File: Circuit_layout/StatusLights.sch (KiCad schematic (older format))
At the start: 30 parts, among them Q1 ZVP4525G, U11 TLP293, U12 TLP293, U16 LTC3638, U2 PS2502-1, U25 TLP293

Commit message: modifying hvpl
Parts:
- removed R17: 250, symbol R
- removed R21: 150, symbol R
- removed U2: PS2502-1, symbol LTV-355T
- added C3: 2.2uF, Capacitors_SMD:C_0805_HandSoldering, symbol C
- added R76: 750k, Resistors_SMD:R_0805_HandSoldering, symbol R
- added R77: 196k, Resistors_SMD:R_0805_HandSoldering, symbol R
- added U1: PDM2-S24-S12, Converters_DCDC_ACDC:DCDC-Conv_TRACO_TMR_1-xxxx_Single, symbol PDM2-S24-S12
- L1: value 220uH -> 100uH; footprint (none) -> Inductors:Inductor_Taiyo-Yuden_NR-80xx_HandSoldering; Description (none) -> FIXED IND 100UH 1A 377 MOHM SMD; DigiKey P/N (none) -> 587-2004-1-ND; Man P/N (none) -> NR8040T101M; Price (none) -> 0.60; URL (none) -> https://www.digikey.com/product-detail/en/taiyo-yuden/NR804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
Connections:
- wire segments 94 -> 97
- no-connect marks 0 -> 1
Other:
- note added: "Need to verify DC DC Conv"
- note added: "Note: this is going to three LEDs"
- note added: "Outputs +12V"
- moved on the sheet: C19
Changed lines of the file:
@@
 LIBS:xilinx
 LIBS:Zilog
-LIBS:pacman-main-cache
 LIBS:bss84
 LIBS:+10v
@@
 Text Label 10250 2450 0    60   ~ 0
 Spare_Blue
-Text Label 8100 5800 2    60   ~ 0
-HVPL
 Text Notes 600  5000 0    60   ~ 0
 High Voltage
@@
 P 5600 5300
 F 0 "L1" V 5550 5300 50  0000 C CNN
-F 1 "220uH" V 5700 5300 50  0000 C CNN
-F 2 "" H 5600 5300 50  0001 C CNN
-F 3 "" H 5600 5300 50  0000 C CNN
+F 1 "100uH" V 5700 5300 50  0000 C CNN
+F 2 "Inductors:Inductor_Taiyo-Yuden_NR-80xx_HandSoldering" H 5600 5300 50  0001 C CNN
+F 3 "http://www.yuden.co.jp/productdata/catalog/en/wound04_e.pdf" H 5600 5300 50  0001 C CNN
+F 4 "587-2004-1-ND" V 5600 5300 60  0001 C CNN "DigiKey P/N"
+F 5 "https://www.digikey.com/product-detail/en/taiyo-yuden/NR8040T101M/587-2004-1-ND/1739117" V 5600 5300 60  0001 C CNN "URL"
+F 6 "NR8040T101M" V 5600 5300 60  0001 C CNN "Man P/N"
+F 7 "FIXED IND 100UH 1A 377 MOHM SMD" V 5600 5300 60  0001 C CNN "Description"
+F 8 "0.60" V 5600 5300 60  0001 C CNN "Price"
 	1    5600 5300
 	0    -1   -1   0
@@
 L C C19
 U 1 1 58BC115E
-P 6200 5750
-F 0 "C19" H 6225 5850 50  0000 L CNN
-F 1 "10uF" H 6225 5650 50  0000 L CNN
-F 2 "Capacitors_SMD:C_0805_HandSoldering" H 6238 5600 50  0001 C CNN
-F 3 "" H 6200 5750 50  0000 C CNN
-F 4 "490-10515-1-ND" H 6200 5750 60  0001 C CNN "DigiKey P/N"
-F 5 "http://www.digikey.com/product-detail/en/murata-electronics-north-america/GRM21BR6YA106ME43L/490-10515-1-ND/5026446" H 6200 5750 60  0001 C CNN "URL"
-F 6 "GRM21BR6YA106ME43L" H 6200 5750 60  0001 C CNN "Man P/N"
-	1    6200 5750
-	1    0    0    -1
-$EndComp
-$Comp
-L LTV-355T U2
-U 1 1 58C27110
-P 7150 5700
-F 0 "U2" H 6940 5890 50  0000 L CNN
-F 1 "PS2502-1" H 7150 5900 50  0000 L CNN
-F 2 "" H 6950 5500 50  0000 L CIN
-F 3 "http://www.cel.com/pdf/datasheets/ps2502.pdf" H 7150 5700 50  0001 L CNN
-F 4 "PS2502L-1-F3-ACT-ND" H 7150 5700 60  0001 C CNN "DigiKey P/N"
-F 5 "http://www.digikey.com/product-detail/en/cel/PS2502L-1-F3-A/PS2502L-1-F3-ACT-ND/3646234" H 7150 5700 60  0001 C CNN "URL"
-F 6 "PS2502L-1-F3-A" H 7150 5700 60  0001 C CNN "Man P/N"
-F 7 "OPTOISOLATOR 5KV DARL 4SMD" H 7150 5700 60  0001 C CNN "Description"
-F 8 "1.10" H 7150 5700 60  0001 C CNN "Price"
-	1    7150 5700
-	1    0    0    -1
-$EndComp
-$Comp
-L R R21
-U 1 1 58C2C36E
-P 7750 5600
-F 0 "R21" V 7830 5600 50  0000 C CNN
-F 1 "150" V 7750 5600 50  0000 C CNN
-F 2 "" V 7680 5600 50  0000 C CNN
-F 3 "" H 7750 5600 50  0000 C CNN
-	1    7750 5600
-	0    1    1    0
-$EndComp
-$Comp
-L +24V #PWR045
-U 1 1 58C2C48F
-P 8050 5500
-F 0 "#PWR045" H 8050 5350 50  0001 C CNN
-F 1 "+24V" H 8050 5640 50  0000 C CNN
-F 2 "" H 8050 5500 50  0000 C CNN
-F 3 "" H 8050 5500 50  0000 C CNN
-	1    8050 5500
-	1    0    0    -1
-$EndComp
-Text Notes 2950 8850 0    60   ~ 0
+P 6600 5750
+F 0 "C19" H 6625 5850 50  0000 L CNN
+F 1 "10uF" H 6625 5650 50  0000 L CNN
+F 2 "Capacitors_SMD:C_0805_HandSoldering" H 6638 5600 50  0001 C CNN
+F 3 "" H 6600 5750 50  0000 C CNN
+F 4 "490-10515-1-ND" H 6600 5750 60  0001 C CNN "DigiKey P/N"
+F 5 "http://www.digikey.com/product-detail/en/murata-electronics-north-america/GRM21BR6YA106ME43L/490-10515-1-ND/5026446" H 6600 5750 60  0001 C CNN "URL"
+F 6 "GRM21BR6YA106ME43L" H 6600 5750 60  0001 C CNN "Man P/N"
+	1    6600 5750
+	1    0    0    -1
+$EndComp
+Text Notes 3550 7400 0    60   ~ 0
 If want to go back to 24V\nsw - 750k - Vfb - 196k - gnd
-$Comp
-L R R17
-U 1 1 58C2FC44
-P 6550 5300
-F 0 "R17" V 6630 5300 50  0000 C CNN
-F 1 "250" V 6550 5300 50  0000 C CNN
-F 2 "" V 6480 5300 50  0000 C CNN
-F 3 "" H 6550 5300 50  0000 C CNN
-	1    6550 5300
-	0    1    1    0
-$EndComp
 Wire Wire Line
 	4250 1200 4350 1200
@@
 	5000 5700 4850 5700
 Wire Wire Line
-	4850 5300 5300 5300
-Wire Wire Line
-	5900 5300 6400 5300
-Wire Wire Line
-	6000 5500 4850 5500
-Wire Wire Line
 	4350 6200 4350 6100
-Wire Wire Line
-	6000 5300 6000 5500
 Wire Wire Line
 	5200 6200 5200 5900
 Connection ~ 5200 6200
-Wire Wire Line
-	5200 5300 5200 5600
-Connection ~ 5200 5300
-Connection ~ 6000 5300
 Wire Notes Line
 	450  4850 11250 4850
-Wire Wire Line
-	7450 5800 8100 5800
-Wire Wire Line
-	7450 5600 7600 5600
-Wire Wire Line
-	7900 5600 8050 5600
-Wire Wire Line
-	8050 5600 8050 5500
-Wire Wire Line
-	6200 6200 6200 5900
 Connection ~ 6200 6200
 Wire Wire Line
-	6200 5600 6200 5300
-Connection ~ 6200 5300
-Wire Wire Line
-	6700 5300 6800 5300
-Wire Wire Line
-	6800 5300 6800 5600
-Wire Wire Line
-	6800 5600 6850 5600
-Wire Wire Line
-	6850 5800 6800 5800
-Wire Wire Line
-	6800 5800 6800 6200
-Wire Wire Line
 	4800 3450 4800 3550
 Wire Wire Line
 	4800 3550 4950 3550
 $Comp
-L +24V #PWR046
+L +24V #PWR045
 U 1 1 58C523A5
 P 4800 2750
-F 0 "#PWR046" H 4800 2600 50  0001 C CNN
+F 0 "#PWR045" H 4800 2600 50  0001 C CNN
 F 1 "+24V" H 4800 2890 50  0000 C CNN
 F 2 "" H 4800 2750 50  0000 C CNN
@@
 $EndComp
 $Comp
-L GND #PWR047
+L GND #PWR046
 U 1 1 58C77294
 P 13700 3000
-F 0 "#PWR047" H 13700 2750 50  0001 C CNN
+F 0 "#PWR046" H 13700 2750 50  0001 C CNN
 F 1 "GND" H 13700 2850 50  0000 C CNN
 F 2 "" H 13700 3000 50  0000 C CNN
@@
 $EndComp
 $Comp
-L +24V #PWR048
+L +24V #PWR047
 U 1 1 58C7729A
 P 15100 2550
-F 0 "#PWR048" H 15100 2400 50  0001 C CNN
+F 0 "#PWR047" H 15100 2400 50  0001 C CNN
 F 1 "+24V" H 15100 2690 50  0000 C CNN
 F 2 "" H 15100 2550 50  0000 C CNN
@@
 HV-
 $Comp
-L PWR_FLAG #FLG049
+L PWR_FLAG #FLG048
 U 1 1 58C1AF3D
 P 3600 5200
-F 0 "#FLG049" H 3600 5295 50  0001 C CNN
+F 0 "#FLG048" H 3600 5295 50  0001 C CNN
 F 1 "PWR_FLAG" H 3600 5380 50  0000 C CNN
 F 2 "" H 3600 5200 50  0000 C CNN
@@
 Connection ~ 3600 5300
 Wire Wire Line
-	6800 6200 700  6200
+	700  6200 7150 6200
 $Comp
 L R R20
@@
 Wire Wire Line
 	1250 1400 1400 1400
+$Comp
+L R R77
+U 1 1 58D32889
+P 6200 5950
+F 0 "R77" V 6280 5950 50  0000 C CNN
+F 1 "196k" V 6200 5950 50  0000 C CNN
+F 2 "Resistors_SMD:R_0805_HandSoldering" V 6130 5950 50  0001 C CNN
+F 3 "" H 6200 5950 50  0000 C CNN
+F 4 "P196CCT-ND" V 6200 5950 60  0001 C CNN "DigiKey P/N"
+F 5 "http://www.digikey.com/product-detail/en/panasonic-electronic-components/ERJ-6ENF1960V/P196CCT-ND/118752" V 6200 5950 60  0001 C CNN "URL"
+F 6 "ERJ-6ENF1960V" V 6200 5950 60  0001 C CNN "Man P/N"
+F 7 "RES SMD 196 OHM 1% 1/8W 0805" V 6200 5950 60  0001 C CNN "Description"
+F 8 "0.1" V 6200 5950 60  0001 C CNN "Price"
+	1    6200 5950
+	1    0    0    -1
+$EndComp
+$Comp
+L R R76
+U 1 1 58D32960
+P 6200 5550
+F 0 "R76" V 6280 5550 50  0000 C CNN
+F 1 "750k" V 6200 5550 50  0000 C CNN
+F 2 "Resistors_SMD:R_0805_HandSoldering" V 6130 5550 50  0001 C CNN
+F 3 "" H 6200 5550 50  0000 C CNN
+F 4 "P750KCCT-ND" V 6200 5550 60  0001 C CNN "DigiKey P/N"
+F 5 "http://www.digikey.com/product-detail/en/panasonic-electronic-components/ERJ-6ENF7503V/P750KCCT-ND/119800" V 6200 5550 60  0001 C CNN "URL"
+F 6 "ERJ-6ENF7503V" V 6200 5550 60  0001 C CNN "Man P/N"
+F 7 "RES SMD 750K OHM 1% 1/8W 0805" V 6200 5550 60  0001 C CNN "Description"
+F 8 "0.1" V 6200 5550 60  0001 C CNN "Price"
+	1    6200 5550
+	1    0    0    -1
+$EndComp
+Wire Wire Line
+	6200 5700 6200 5800
+Wire Wire Line
+	4850 5300 5300 5300
+Wire Wire Line
+	5200 5600 5200 5300
+Connection ~ 5200 5300
+Wire Wire Line
+	5900 5300 7150 5300
+Wire Wire Line
+	6200 5300 6200 5400
+Wire Wire Line
+	6200 6100 6200 6200
+Connection ~ 6200 5300
+Wire Wire Line
+	6600 5300 6600 5600
+Wire Wire Line
+	6600 5900 6600 6200
+Connection ~ 6600 6200
+Connection ~ 6600 5300
+$Comp
+L PDM2-S24-S12 U1
+U 1 1 58D3B6C8
+P 7900 5700
+F 0 "U1" H 7900 5600 50  0000 C CNN
+F 1 "PDM2-S24-S12" H 7900 5900 50  0000 C CNN
+F 2 "Converters_DCDC_ACDC:DCDC-Conv_TRACO_TMR_1-xxxx_Single" H 7900 5300 50  0001 C CNN
+F 3 "" H 7900 5200 50  0001 C CNN
+F 4 "102-2728-ND" H 7900 5700 60  0001 C CNN "DigiKey P/N"
+F 5 "https://www.digikey.com/product-detail/en/cui-inc/PDM2-S24-S12-S/102-2728-ND/4009652" H 7900 5700 60  0001 C CNN "URL"
+F 6 "PDM2-S24-S12-S" H 7900 5700 60  0001 C CNN "Man P/N"
+F 7 "CONVERT DC/DC 2W 12V 167MA OUT" H 7900 5700 60  0001 C CNN "Description"
+	1    7900 5700
+	1    0    0    -1
+$EndComp
+Wire Wire Line
+	7150 5300 7150 5600
+Wire Wire Line
+	7150 5800 7150 5800
+Wire Wire Line
+	7150 6200 7150 5800
+NoConn ~ 8650 5700
+$Comp
+L GND #PWR049
+U 1 1 58D3C796
+P 9400 5950
+F 0 "#PWR049" H 9400 5700 50  0001 C CNN
+F 1 "GND" H 9400 5800 50  0000 C CNN
+F 2 "" H 9400 5950 50  0000 C CNN
+F 3 "" H 9400 5950 50  0000 C CNN
+	1    9400 5950
+	1    0    0    -1
+$EndComp
+Text Label 9500 5550 2    60   ~ 0
+HVPL
+Text Notes 8550 5400 0    60   ~ 0
+Note: this is going to three LEDs
+Text Notes 7350 6200 0    60   ~ 0
+Need to verify DC DC Conv
+$Comp
+L C C3
+U 1 1 58D40888
+P 9000 5700
+F 0 "C3" H 9025 5800 50  0000 L CNN
+F 1 "2.2uF" H 9025 5600 50  0000 L CNN
+F 2 "Capacitors_SMD:C_0805_HandSoldering" H 9038 5550 50  0001 C CNN
+F 3 "" H 9000 5700 50  0000 C CNN
+F 4 "587-1293-1-ND" H 9000 5700 60  0001 C CNN "DigiKey P/N"
+F 5 "http://www.digikey.com/product-detail/en/taiyo-yuden/EMK212BJ225KG-T/587-1293-1-ND/931070" H 9000 5700 60  0001 C CNN "URL"
+F 6 "EMK212BJ225KG-T" H 9000 5700 60  0001 C CNN "Man P/N"
+F 7 "CAP CER 2.2UF 16V X5R 0805" H 9000 5700 60  0001 C CNN "Description"
+	1    9000 5700
+	1    0    0    -1
+$EndComp
+Text Notes 7600 5350 0    60   ~ 0
+Outputs +12V
+Wire Wire Line
+	8650 5800 8650 5850
+Wire Wire Line
+	8650 5850 9400 5850
+Wire Wire Line
+	8650 5600 8650 5550
+Wire Wire Line
+	8650 5550 9500 5550
+Connection ~ 9000 5550
+Wire Wire Line
+	9400 5850 9400 5950
+Connection ~ 9000 5850
+Wire Wire Line
+	4850 5500 6000 5500
+Wire Wire Line
+	6000 5500 6000 5750
+Wire Wire Line
+	6000 5750 6200 5750
+Connection ~ 6200 5750
 $EndSCHEMATC

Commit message: added footprint to DPDT switch, test points, DRC passes
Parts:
- removed R75: 150, Resistors_SMD:R_0805_HandSoldering, symbol R
- removed U25: TLP293, Housings_SSOP:SOP-4_4.4x2.8mm_Pitch1.27mm, symbol TLP291
- added HVPL_HV: TEST_1P, Measurement_Points:Measurement_Point_Round-SMD-Pad_Big, symbol TEST_1P
- added W?: HVPL_LV, Measurement_Points:Measurement_Point_Round-SMD-Pad_Big, symbol TEST_1P
- added W?: GLV_GND, Measurement_Points:Measurement_Point_Square-SMD-Pad_Big, symbol TEST_1P
- added W?: HV_GND, Measurement_Points:Measurement_Point_Square-SMD-Pad_Big, symbol TEST_1P
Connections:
- net GND: now also W?.1
- net HV-: now also W?.1
- net HVPL: now also W?.1
- net at C19.1, L1.2, R76.1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: now also HVPL_HV.1
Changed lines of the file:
@@
 LIBS:xilinx
 LIBS:Zilog
+LIBS:pacman-main-cache
 LIBS:bss84
 LIBS:+10v
@@
 $EndComp
 $Comp
-L GND #PWR036
+L GND #PWR037
 U 1 1 58AF33D9
 P 4250 1300
-F 0 "#PWR036" H 4250 1050 50  0001 C CNN
+F 0 "#PWR037" H 4250 1050 50  0001 C CNN
 F 1 "GND" H 4250 1150 50  0000 C CNN
 F 2 "" H 4250 1300 50  0000 C CNN
@@
 $EndComp
 $Comp
-L +24V #PWR037
+L +24V #PWR038
 U 1 1 58AF3526
 P 5650 850
-F 0 "#PWR037" H 5650 700 50  0001 C CNN
+F 0 "#PWR038" H 5650 700 50  0001 C CNN
 F 1 "+24V" H 5650 990 50  0000 C CNN
 F 2 "" H 5650 850 50  0000 C CNN
@@
 $EndComp
 $Comp
-L GND #PWR038
+L GND #PWR039
 U 1 1 58AF4273
 P 4250 2500
-F 0 "#PWR038" H 4250 2250 50  0001 C CNN
+F 0 "#PWR039" H 4250 2250 50  0001 C CNN
 F 1 "GND" H 4250 2350 50  0000 C CNN
 F 2 "" H 4250 2500 50  0000 C CNN
@@
 $EndComp
 $Comp
-L +24V #PWR039
+L +24V #PWR040
 U 1 1 58AF427B
 P 5650 2000
-F 0 "#PWR039" H 5650 1850 50  0001 C CNN
+F 0 "#PWR040" H 5650 1850 50  0001 C CNN
 F 1 "+24V" H 5650 2140 50  0000 C CNN
 F 2 "" H 5650 2000 50  0000 C CNN
@@
 $EndComp
 $Comp
-L GND #PWR040
+L GND #PWR041
 U 1 1 58B26825
 P 8750 1200
-F 0 "#PWR040" H 8750 950 50  0001 C CNN
+F 0 "#PWR041" H 8750 950 50  0001 C CNN
 F 1 "GND" H 8750 1050 50  0000 C CNN
 F 2 "" H 8750 1200 50  0000 C CNN
@@
 $EndComp
 $Comp
-L GND #PWR041
+L GND #PWR042
 U 1 1 58B26F4E
 P 8750 1650
-F 0 "#PWR041" H 8750 1400 50  0001 C CNN
+F 0 "#PWR042" H 8750 1400 50  0001 C CNN
 F 1 "GND" H 8750 1500 50  0000 C CNN
 F 2 "" H 8750 1650 50  0000 C CNN
@@
 $EndComp
 $Comp
-L GND #PWR042
+L GND #PWR043
 U 1 1 58B272AA
 P 8750 2100
-F 0 "#PWR042" H 8750 1850 50  0001 C CNN
+F 0 "#PWR043" H 8750 1850 50  0001 C CNN
 F 1 "GND" H 8750 1950 50  0000 C CNN
 F 2 "" H 8750 2100 50  0000 C CNN
@@
 $EndComp
 $Comp
-L GND #PWR043
+L GND #PWR044
 U 1 1 58B27330
 P 8750 2550
-F 0 "#PWR043" H 8750 2300 50  0001 C CNN
+F 0 "#PWR044" H 8750 2300 50  0001 C CNN
 F 1 "GND" H 8750 2400 50  0000 C CNN
 F 2 "" H 8750 2550 50  0000 C CNN
@@
 Blue
 $Comp
-L +5V #PWR044
+L +5V #PWR045
 U 1 1 58B2809B
 P 10250 1100
-F 0 "#PWR044" H 10250 950 50  0001 C CNN
+F 0 "#PWR045" H 10250 950 50  0001 C CNN
 F 1 "+5V" H 10250 1240 50  0000 C CNN
 F 2 "" H 10250 1100 50  0000 C CNN
@@
 	5200 6200 5200 5900
 Connection ~ 5200 6200
-Wire Notes Line
-	450  4850 11250 4850
 Connection ~ 6200 6200
 Wire Wire Line
@@
 	4800 3550 4950 3550
 $Comp
-L +24V #PWR045
+L +24V #PWR046
 U 1 1 58C523A5
 P 4800 2750
-F 0 "#PWR045" H 4800 2600 50  0001 C CNN
+F 0 "#PWR046" H 4800 2600 50  0001 C CNN
 F 1 "+24V" H 4800 2890 50  0000 C CNN
 F 2 "" H 4800 2750 50  0000 C CNN
@@
 	1    0    0    -1
 $EndComp
-$Comp
-L TLP291 U25
-U 1 1 58C7728E
-P 14050 2800
-F 0 "U25" H 13850 3000 50  0000 L CNN
-F 1 "TLP293" H 14050 3000 50  0000 L CNN
-F 2 "Housings_SSOP:SOP-4_4.4x2.8mm_Pitch1.27mm" H 13850 2600 50  0001 L CIN
-F 3 "" H 14050 2800 50  0000 L CNN
-F 4 "TLP293(GB-TPLECT-ND" H 14050 2800 60  0001 C CNN "DigiKey P/N"
-F 5 "http://www.digikey.com/product-detail/en/toshiba-semiconductor-and-storage/TLP293(GB-TPL,E/TLP293(GB-TPLECT-ND/4562965" H 14050 2800 60  0001 C CNN "URL"
-F 6 "TLP293(GB-TPLE" H 14050 2800 60  0001 C CNN "Man P/N"
-F 7 "http://www.digikey.com/product-detail/en/toshiba-semiconductor-and-storage/TLP291(GB-TP,SE/TLP291(GB-TPSECT-ND/4562949" H 14050 2800 60  0001 C CNN "TLP291"
-	1    14050 2800
-	1    0    0    -1
-$EndComp
-$Comp
-L GND #PWR046
-U 1 1 58C77294
-P 13700 3000
-F 0 "#PWR046" H 13700 2750 50  0001 C CNN
-F 1 "GND" H 13700 2850 50  0000 C CNN
-F 2 "" H 13700 3000 50  0000 C CNN
-F 3 "" H 13700 3000 50  0000 C CNN
-	1    13700 3000
-	1    0    0    -1
-$EndComp
-$Comp
-L +24V #PWR047
-U 1 1 58C7729A
-P 15100 2550
-F 0 "#PWR047" H 15100 2400 50  0001 C CNN
-F 1 "+24V" H 15100 2690 50  0000 C CNN
-F 2 "" H 15100 2550 50  0000 C CNN
-F 3 "" H 15100 2550 50  0000 C CNN
-	1    15100 2550
-	1    0    0    -1
-$EndComp
-$Comp
-L R R75
-U 1 1 58C772A3
-P 13350 2700
-F 0 "R75" V 13430 2700 50  0000 C CNN
-F 1 "150" V 13350 2700 50  0000 C CNN
-F 2 "Resistors_SMD:R_0805_HandSoldering" V 13280 2700 50  0001 C CNN
-F 3 "" H 13350 2700 50  0000 C CNN
-F 4 "311-150CRCT-ND" V 13350 2700 60  0001 C CNN "DigiKey P/N"
-F 5 "http://www.digikey.com/product-detail/en/yageo/RC0805FR-07150RL/311-150CRCT-ND/730560" V 13350 2700 60  0001 C CNN "URL"
-F 6 "RC0805FR-07150RL" V 13350 2700 60  0001 C CNN "Man P/N"
-	1    13350 2700
-	0    1    1    0
-$EndComp
-Wire Wire Line
-	13700 2900 13750 2900
-Wire Wire Line
-	13750 2700 13500 2700
-Wire Wire Line
-	13700 2900 13700 3000
-Wire Wire Line
-	14350 2700 15100 2700
-Wire Wire Line
-	14350 2900 14850 2900
-Wire Wire Line
-	13200 2700 12700 2700
-Wire Wire Line
-	15100 2700 15100 2550
-Text Label 14850 2900 0    60   ~ 0
-IMD_Fault_LED
-Text Label 12700 2700 0    60   ~ 0
-IMD_Status
 Wire Wire Line
 	4350 3200 4500 3200
@@
 HV-
 $Comp
-L PWR_FLAG #FLG048
+L PWR_FLAG #FLG049
 U 1 1 58C1AF3D
 P 3600 5200
-F 0 "#FLG048" H 3600 5295 50  0001 C CNN
+F 0 "#FLG049" H 3600 5295 50  0001 C CNN
 F 1 "PWR_FLAG" H 3600 5380 50  0000 C CNN
 F 2 "" H 3600 5200 50  0000 C CNN
@@
 NoConn ~ 8650 5700
 $Comp
-L GND #PWR049
+L GND #PWR050
 U 1 1 58D3C796
 P 9400 5950
-F 0 "#PWR049" H 9400 5700 50  0001 C CNN
+F 0 "#PWR050" H 9400 5700 50  0001 C CNN
 F 1 "GND" H 9400 5800 50  0000 C CNN
 F 2 "" H 9400 5950 50  0000 C CNN
@@
 Text Label 9500 5550 2    60   ~ 0
 HVPL
-Text Notes 8550 5400 0    60   ~ 0
+Text Notes 9550 5750 0    60   ~ 0
 Note: this is going to three LEDs
-Text Notes 7350 6200 0    60   ~ 0
+Text Notes 8000 6400 0    60   ~ 0
 Need to verify DC DC Conv
 $Comp
@@
 	6000 5750 6200 5750
 Connection ~ 6200 5750
+Wire Notes Line
+	7900 6500 7900 4850
+Wire Notes Line
+	7900 4850 500  4850
+$Comp
+L TEST_1P W?
+U 1 1 58D48101
+P 8800 5450
+F 0 "W?" H 8800 5720 50  0000 C CNN
+F 1 "HVPL_LV" H 8800 5650 50  0000 C CNN
+F 2 "Measurement_Points:Measurement_Point_Round-SMD-Pad_Big" H 9000 5450 50  0001 C CNN
+F 3 "" H 9000 5450 50  0000 C CNN
+	1    8800 5450
+	1    0    0    -1
+$EndComp
+$Comp
+L TEST_1P W?
+U 1 1 58D48194
+P 8800 5950
+F 0 "W?" H 8800 6220 50  0000 C CNN
+F 1 "GLV_GND" H 8800 6150 50  0000 C CNN
+F 2 "Measurement_Points:Measurement_Point_Square-SMD-Pad_Big" H 9000 5950 50  0001 C CNN
+F 3 "" H 9000 5950 50  0000 C CNN
+	1    8800 5950
+	-1   0    0    1
+$EndComp
+Wire Wire Line
+	8800 5950 8800 5850
+Connection ~ 8800 5850
+Wire Wire Line
+	8800 5450 8800 5550
+Connection ~ 8800 5550
+$Comp
+L TEST_1P W?
+U 1 1 58D48B52
+P 6750 6300
+F 0 "W?" H 6750 6570 50  0000 C CNN
+F 1 "HV_GND" H 6750 6500 50  0000 C CNN
+F 2 "Measurement_Points:Measurement_Point_Square-SMD-Pad_Big" H 6950 6300 50  0001 C CNN
+F 3 "" H 6950 6300 50  0000 C CNN
+	1    6750 6300
+	-1   0    0    1
+$EndComp
+$Comp
+L TEST_1P HVPL_HV
+U 1 1 58D48C4B
+P 6800 5200
+F 0 "HVPL_HV" H 6800 5470 50  0000 C CNN
+F 1 "TEST_1P" H 6800 5400 50  0000 C CNN
+F 2 "Measurement_Points:Measurement_Point_Round-SMD-Pad_Big" H 7000 5200 50  0001 C CNN
+F 3 "" H 7000 5200 50  0000 C CNN
+	1    6800 5200
+	1    0    0    -1
+$EndComp
+Wire Wire Line
+	6750 6300 6750 6200
+Connection ~ 6750 6200
+Wire Wire Line
+	6800 5200 6800 5300
+Connection ~ 6800 5300
 $EndSCHEMATC

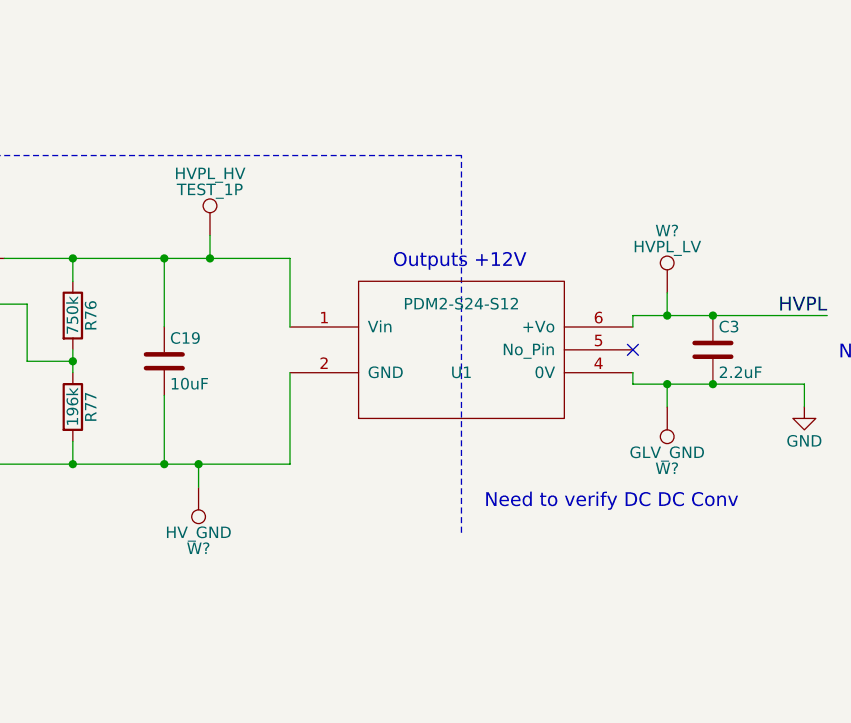
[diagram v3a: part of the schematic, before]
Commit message: cleaned up footprints of more testpoints. ran DRC again, passed
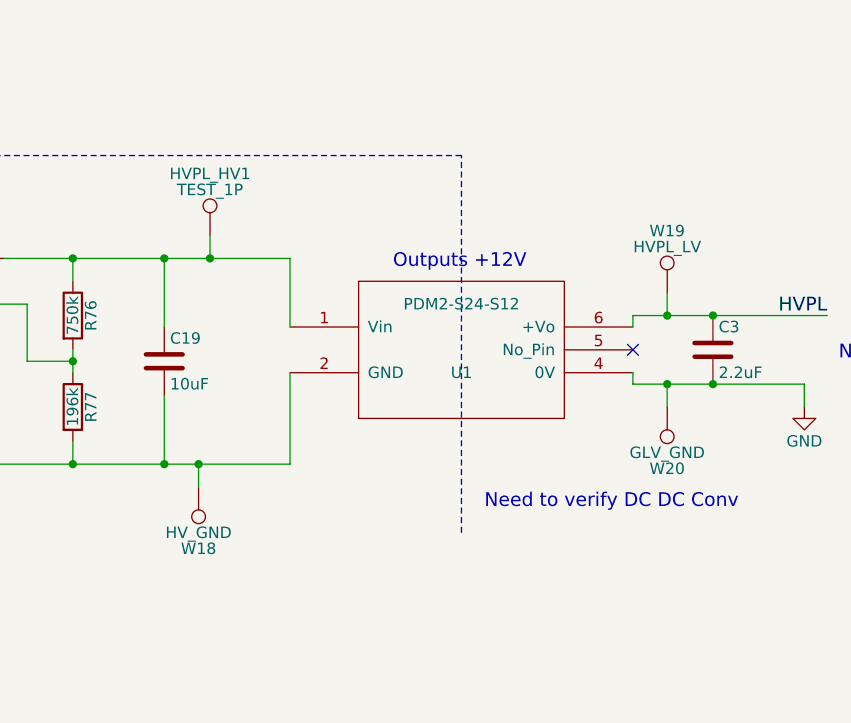
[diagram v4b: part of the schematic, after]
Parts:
- gave numbers to parts that had none: 3
- renumbered HVPL_HV to HVPL_HV1
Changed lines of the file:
@@
 HV-
 $Comp
-L PWR_FLAG #FLG049
+L PWR_FLAG #FLG047
 U 1 1 58C1AF3D
 P 3600 5200
-F 0 "#FLG049" H 3600 5295 50  0001 C CNN
+F 0 "#FLG047" H 3600 5295 50  0001 C CNN
 F 1 "PWR_FLAG" H 3600 5380 50  0000 C CNN
 F 2 "" H 3600 5200 50  0000 C CNN
@@
 NoConn ~ 8650 5700
 $Comp
-L GND #PWR050
+L GND #PWR048
 U 1 1 58D3C796
 P 9400 5950
-F 0 "#PWR050" H 9400 5700 50  0001 C CNN
+F 0 "#PWR048" H 9400 5700 50  0001 C CNN
 F 1 "GND" H 9400 5800 50  0000 C CNN
 F 2 "" H 9400 5950 50  0000 C CNN
@@
 	7900 4850 500  4850
 $Comp
-L TEST_1P W?
+L TEST_1P W19
 U 1 1 58D48101
 P 8800 5450
-F 0 "W?" H 8800 5720 50  0000 C CNN
+F 0 "W19" H 8800 5720 50  0000 C CNN
 F 1 "HVPL_LV" H 8800 5650 50  0000 C CNN
 F 2 "Measurement_Points:Measurement_Point_Round-SMD-Pad_Big" H 9000 5450 50  0001 C CNN
@@
 $EndComp
 $Comp
-L TEST_1P W?
+L TEST_1P W20
 U 1 1 58D48194
 P 8800 5950
-F 0 "W?" H 8800 6220 50  0000 C CNN
+F 0 "W20" H 8800 6220 50  0000 C CNN
 F 1 "GLV_GND" H 8800 6150 50  0000 C CNN
 F 2 "Measurement_Points:Measurement_Point_Square-SMD-Pad_Big" H 9000 5950 50  0001 C CNN
@@
 Connection ~ 8800 5550
 $Comp
-L TEST_1P W?
+L TEST_1P W18
 U 1 1 58D48B52
 P 6750 6300
-F 0 "W?" H 6750 6570 50  0000 C CNN
+F 0 "W18" H 6750 6570 50  0000 C CNN
 F 1 "HV_GND" H 6750 6500 50  0000 C CNN
 F 2 "Measurement_Points:Measurement_Point_Square-SMD-Pad_Big" H 6950 6300 50  0001 C CNN
@@
 $EndComp
 $Comp
-L TEST_1P HVPL_HV
+L TEST_1P HVPL_HV1
 U 1 1 58D48C4B
 P 6800 5200
-F 0 "HVPL_HV" H 6800 5470 50  0000 C CNN
+F 0 "HVPL_HV1" H 6800 5470 50  0000 C CNN
 F 1 "TEST_1P" H 6800 5400 50  0000 C CNN
 F 2 "Measurement_Points:Measurement_Point_Round-SMD-Pad_Big" H 7000 5200 50  0001 C CNN
